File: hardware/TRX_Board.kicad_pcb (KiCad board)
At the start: 4 copper layers, 35.1 x 62.7 mm, 60 parts, among them J1 Conn_02x08_Odd_Even, J2 SMA, J3 Conn_01x03, J4 Conn_01x03, Q1 BSN20, Q2 BSN20, Q3 BSN20, U1 AP1117-33, U2 LM386, U3 DRA818U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

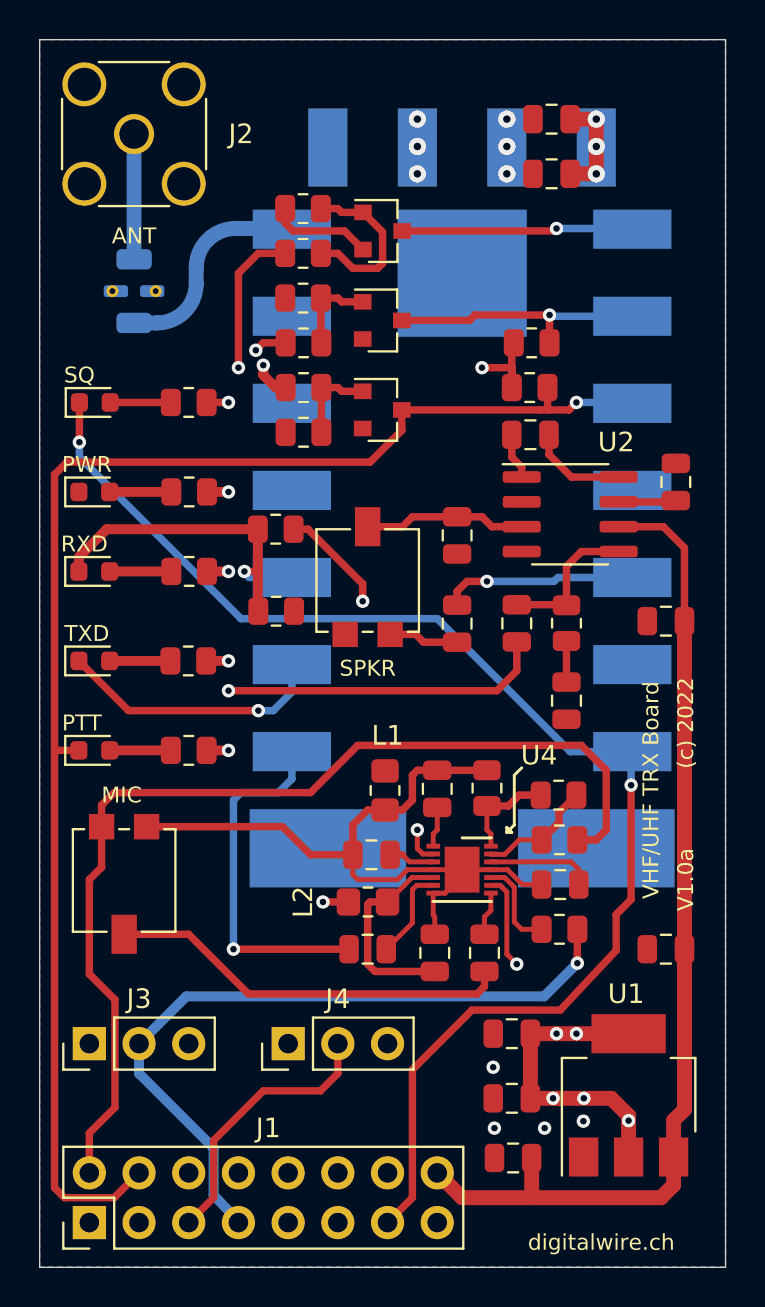
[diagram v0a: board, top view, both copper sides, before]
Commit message: Optimized MIC path for electret and digital sources / added separated dirs for Gerbers
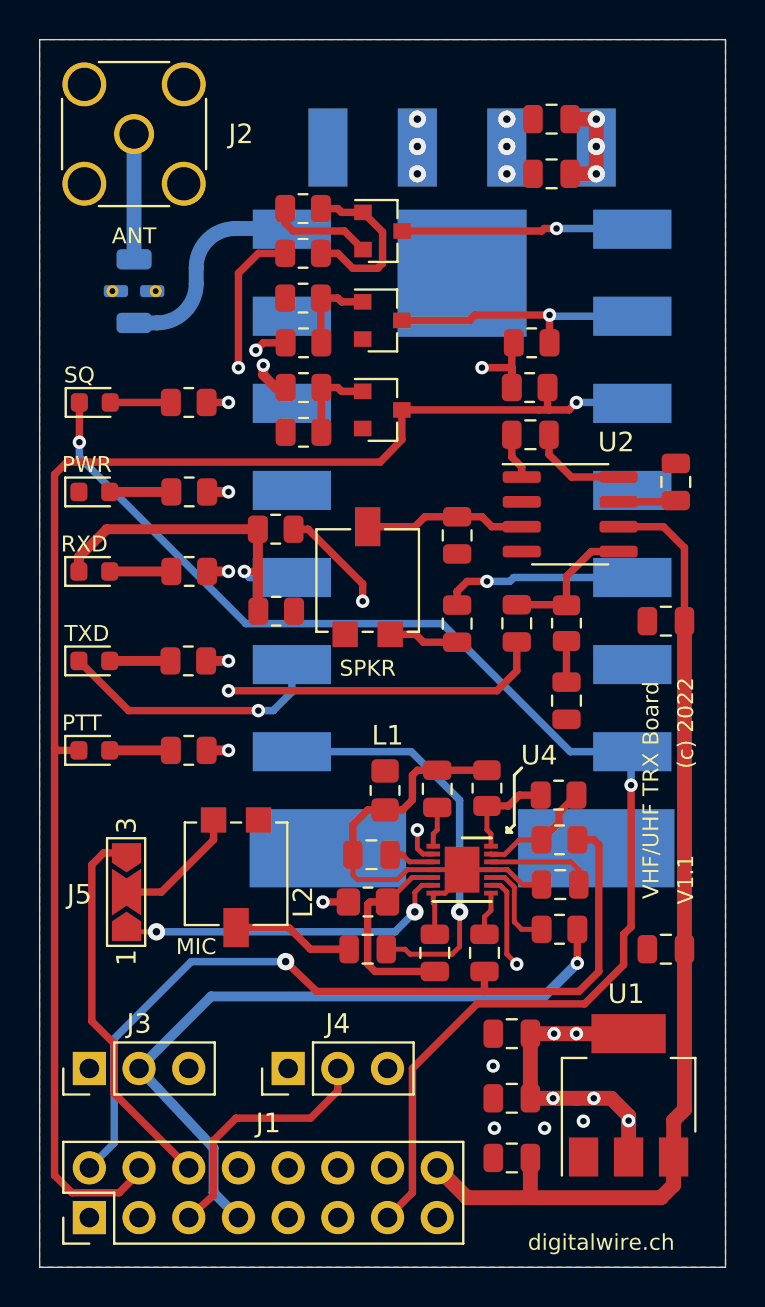
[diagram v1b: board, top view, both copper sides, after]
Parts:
- added J5: Conn_01x03, Jumper:SolderJumper-3_P2.0mm_Open_TrianglePad1.0x1.5mm_NumberLabels, F.Cu at (109.9, 107.8)
- moved RV2 5.73 mm to (115.5, 106.9)
- moved J3 1.27 mm to (108.0, 116.8)
- moved J4 1.27 mm to (118.1, 116.8)
- moved J1 0.25 mm to (108.0, 124.5)
- moved C2 0.07 mm to (129.5, 121.4)
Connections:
- C15 pad 2: Net-(C15-Pad2) -> /MIC-AMP_IN
- C19 pad 2: /MIC_TRX -> Net-(C19-Pad2)
- J1 pad 2: /MIC -> /MIC-AMP_IN
- J1 pad 6: /MIC_TRX -> /MIC-DIGI_IN
- R14 pad 2: /MIC -> /MIC-AMP_IN
- RV2 pad 1: /MIC -> /TRX_MIC
- RV2 pad 2: Net-(C15-Pad2) -> Net-(C19-Pad2)
- RV2 pad 3: Net-(C11-Pad1) -> GND
- U3 pad 11: Net-(U3-Pad11) -> unconnected-(U3-Pad11)
- U3 pad 13: Net-(U3-Pad13) -> unconnected-(U3-Pad13)
- U3 pad 14: Net-(U3-Pad14) -> unconnected-(U3-Pad14)
- U3 pad 15: Net-(U3-Pad15) -> unconnected-(U3-Pad15)
- U3 pad 18: /MIC_TRX -> Net-(C19-Pad1)
- U3 pad 2: Net-(U3-Pad2) -> unconnected-(U3-Pad2)
- U3 pad 4: Net-(U3-Pad4) -> unconnected-(U3-Pad4)
- U4 pad 6: Net-(C19-Pad1) -> Net-(U4-Pad6)
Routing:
- net /MIC: track 52.4 -> 0.00 mm
- net /MIC-AMP_IN: track 0.00 -> 43.3 mm, vias 0 -> 1
- net /MIC_TRX: track 30.7 -> 0.00 mm, vias 1 -> 0
- net Net-(C15-Pad2): track 20.6 -> 0.00 mm
- net /MIC-DIGI_IN: track 0.00 -> 19.6 mm
- net Net-(U4-Pad6): track 0.00 -> 17.3 mm, vias 0 -> 2
- net Net-(C19-Pad1): track 4.76 -> 21.1 mm, vias 0 -> 1
- net Net-(C11-Pad1): track 37.0 -> 25.9 mm
- net /TRX_MIC: track 0.00 -> 6.57 mm
- net Net-(C19-Pad2): track 0.00 -> 6.23 mm
- net /-SLEEP: track 45.8 -> 44.3 mm
- net /*RFPWR: track 54.4 -> 53.2 mm
- net /MIC_GAIN: track 37.1 -> 36.0 mm
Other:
- board text added: "V1.1"
- board text removed: "V1.0a"
